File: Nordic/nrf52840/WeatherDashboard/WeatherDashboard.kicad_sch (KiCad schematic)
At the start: 0 parts

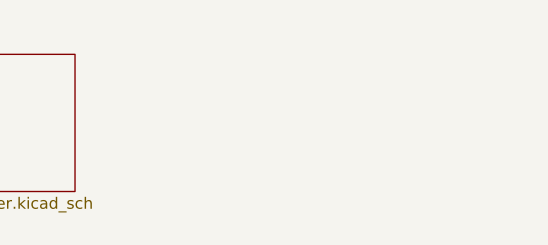
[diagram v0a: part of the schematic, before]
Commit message: power and display
Added power regulator and start populating display components
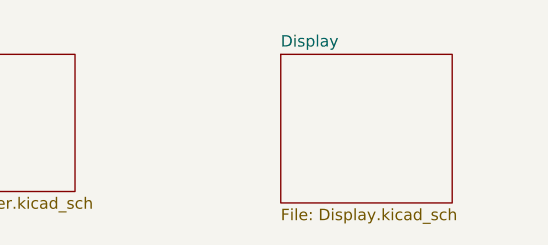
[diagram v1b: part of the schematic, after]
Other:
- added sheet Display (Display.kicad_sch)
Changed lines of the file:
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@@
+	)
+	(sheet
+		(at 181.61 77.47)
+		(size 19.05 16.51)
+		(exclude_from_sim no)
+		(in_bom yes)
+		(on_board yes)
+		(dnp no)
+		(fields_autoplaced yes)
+		(stroke
+			(width 0.1524)
+			(type solid)
+		)
+		(fill
+			(color 0 0 0 0.0000)
+		)
+		(property "Sheetname" "Display"
+			(at 181.61 76.7584 0)
+			(effects
+				(font
+					(size 1.27 1.27)
+				)
+				(justify left bottom)
+			)
+		)
+		(property "Sheetfile" "Display.kicad_sch"
+			(at 181.61 94.5646 0)
+			(effects
+				(font
+					(size 1.27 1.27)
+				)
+				(justify left top)
+			)
+		)
+		(instances
+			(project "WeatherDashboard"
+				(path "/189808bb-364f-4c11-a922-cc9d9f33a674"
+					(page "4")
+				)
+			)
+		)
 	)
 	(sheet

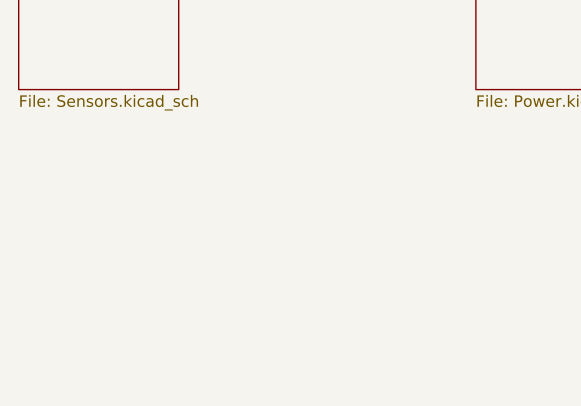
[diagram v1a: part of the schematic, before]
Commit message: pcie
added pcie connector
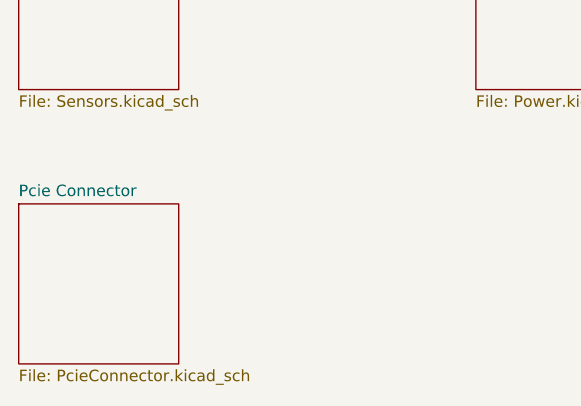
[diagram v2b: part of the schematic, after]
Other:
- added sheet Pcie Connector (PcieConnector.kicad_sch)
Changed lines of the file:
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@@
 	(paper "A4")
+	(sheet
+		(at 91.44 105.41)
+		(size 17.78 17.78)
+		(exclude_from_sim no)
+		(in_bom yes)
+		(on_board yes)
+		(dnp no)
+		(fields_autoplaced yes)
+		(stroke
+			(width 0.1524)
+			(type solid)
+		)
+		(fill
+			(color 0 0 0 0.0000)
+		)
+		(property "Sheetname" "Pcie Connector"
+			(at 91.44 104.6984 0)
+			(effects
+				(font
+					(size 1.27 1.27)
+				)
+				(justify left bottom)
+			)
+		)
+		(property "Sheetfile" "PcieConnector.kicad_sch"
+			(at 91.44 123.7746 0)
+			(effects
+				(font
+					(size 1.27 1.27)
+				)
+				(justify left top)
+			)
+		)
+		(instances
+			(project "WeatherDashboard"
+				(path "/189808bb-364f-4c11-a922-cc9d9f33a674"
+					(page "5")
+				)
+			)
+		)
+	)
 	(sheet
 		(at 142.24 77.47)

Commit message: pcie connector
Add connectins to the pcie connector
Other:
- sheet Display ports: added 3v3, 3v3_EN, BS, EPD_BUSY, EPD_DC, EPD_DIN, EPD_SCK, GND, TSCL, TSDA, ~{EPD_CS}, ~{EPD_RST}; removed none
- sheet Pcie Connector ports: added 3v3, EPD_BUSY, EPD_DC, EPD_DIN, EPD_SCK, GND, SCL, SDA, ~{EPD_CS}, ~{EPD_RST}; removed none
- sheet Power ports: added 3v3, GND; removed none
- sheet Sensors ports: added 3v3, GND, SCL, SDA; removed none

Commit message: Layout
layout update
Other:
- sheet Display ports: added none; removed BS
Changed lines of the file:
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@@
 	(paper "A4")
+	(junction
+		(at 152.4 73.66)
+		(diameter 0)
+		(color 0 0 0 0)
+	)
 	(junction
 		(at 138.43 100.33)
@@
 	(wire
 		(pts
+			(xy 152.4 76.2) (xy 152.4 73.66)
+		)
+		(stroke
+			(width 0)
+			(type default)
+		)
+	)
+	(wire
+		(pts
 			(xy 138.43 129.54) (xy 138.43 100.33)
 		)
@@
 	(wire
 		(pts
+			(xy 154.94 76.2) (xy 152.4 76.2)
+		)
+		(stroke
+			(width 0)
+			(type default)
+		)
+	)
+	(wire
+		(pts
 			(xy 135.89 102.87) (xy 154.94 102.87)
 		)
@@
 	(wire
 		(pts
-			(xy 130.81 73.66) (xy 154.94 73.66)
+			(xy 130.81 73.66) (xy 152.4 73.66)
 		)
 		(stroke
@@
 		(pts
 			(xy 124.46 102.87) (xy 135.89 102.87)
+		)
+		(stroke
+			(width 0)
+			(type default)
+		)
+	)
+	(wire
+		(pts
+			(xy 152.4 73.66) (xy 154.94 73.66)
 		)
 		(stroke
@@
 			(effects
 				(font
-					(size 1.27 1.27)
-				)
-				(justify left)
-			)
-		)
-		(pin "BS" input
-			(at 154.94 95.25 180)
-			(effects
-				(font

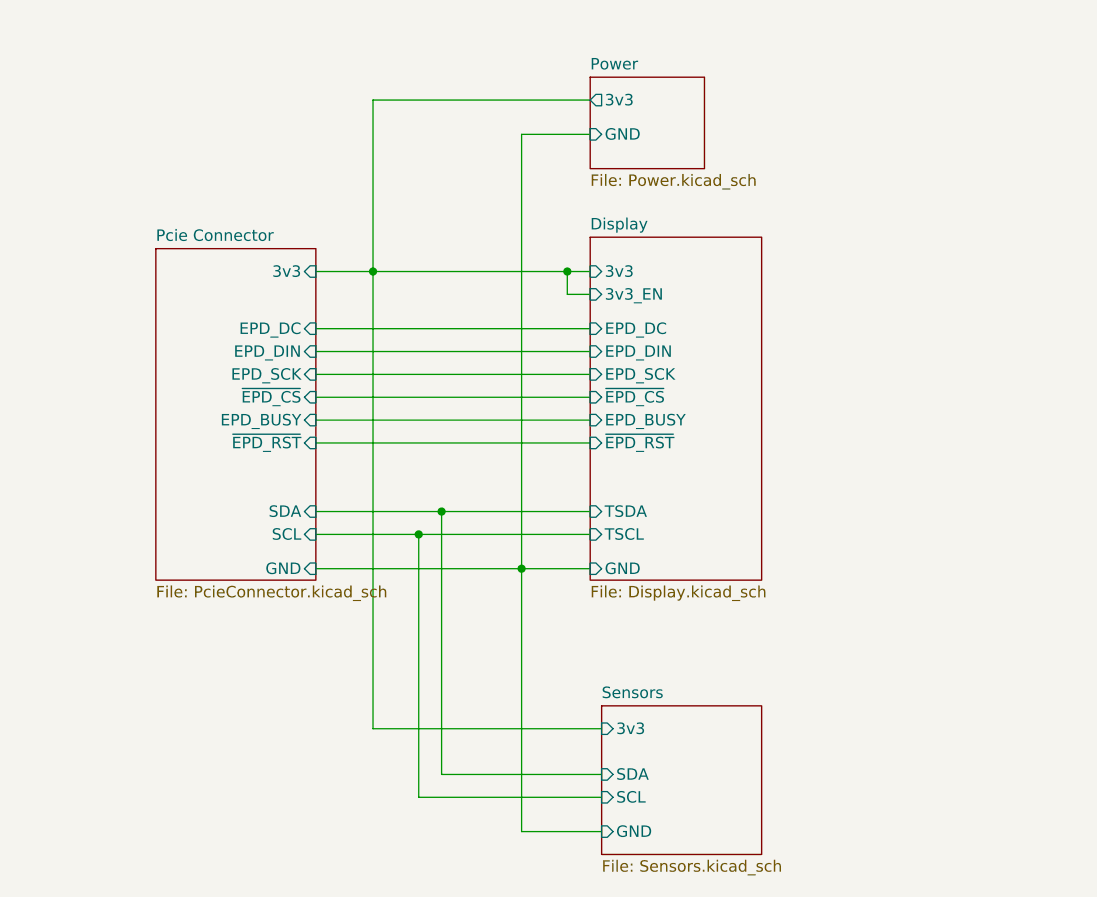
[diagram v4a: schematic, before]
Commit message: layout
Start weather station layout
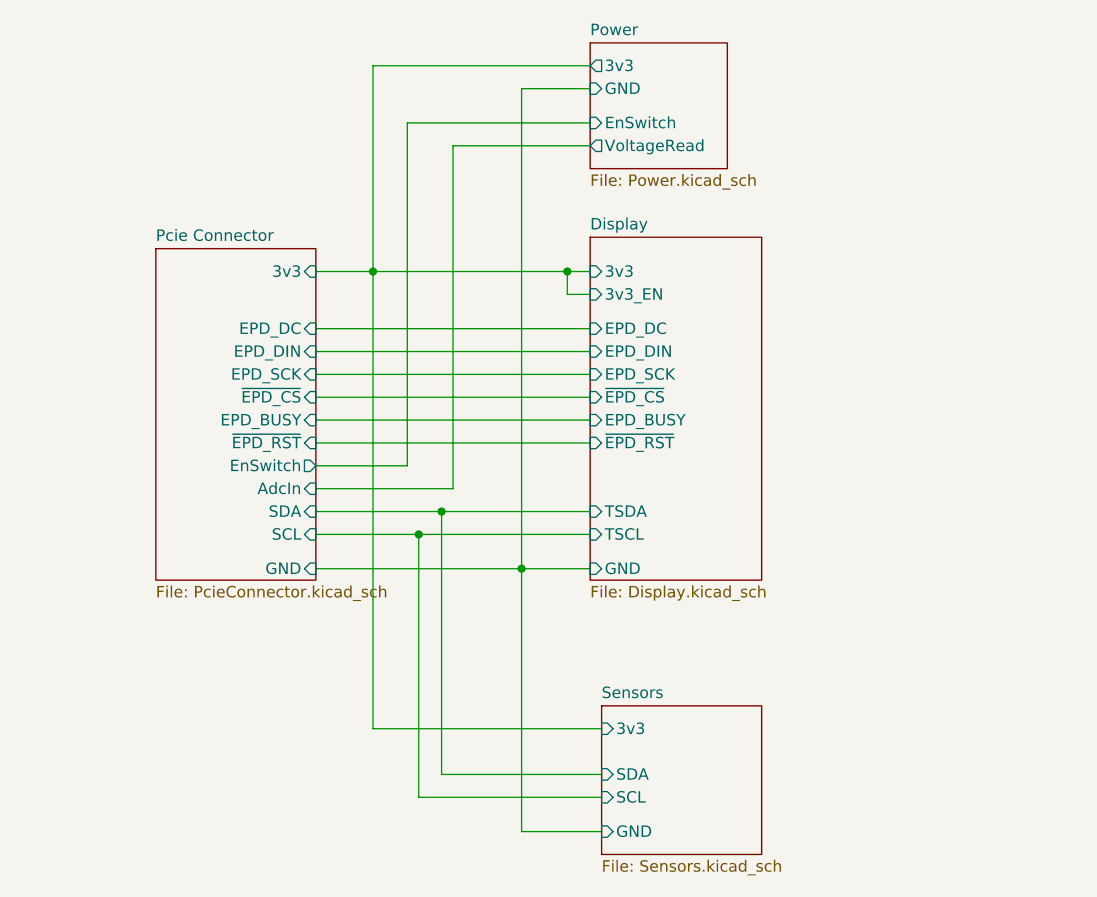
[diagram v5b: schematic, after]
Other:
- sheet Pcie Connector ports: added AdcIn, EnSwitch; removed none
- sheet Power ports: added EnSwitch, VoltageRead; removed none
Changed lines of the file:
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@@
 	(wire
 		(pts
-			(xy 154.94 58.42) (xy 147.32 58.42)
+			(xy 154.94 53.34) (xy 147.32 53.34)
+		)
+		(stroke
+			(width 0)
+			(type default)
+		)
+	)
+	(wire
+		(pts
+			(xy 139.7 59.69) (xy 154.94 59.69)
+		)
+		(stroke
+			(width 0)
+			(type default)
+		)
+	)
+	(wire
+		(pts
+			(xy 134.62 57.15) (xy 134.62 95.25)
 		)
 		(stroke
@@
 	(wire
 		(pts
-			(xy 154.94 54.61) (xy 130.81 54.61)
+			(xy 154.94 50.8) (xy 130.81 50.8)
 		)
 		(stroke
@@
 	(wire
 		(pts
-			(xy 147.32 58.42) (xy 147.32 106.68)
+			(xy 147.32 53.34) (xy 147.32 106.68)
 		)
 		(stroke
@@
 	(wire
 		(pts
+			(xy 124.46 97.79) (xy 139.7 97.79)
+		)
+		(stroke
+			(width 0)
+			(type default)
+		)
+	)
+	(wire
+		(pts
 			(xy 135.89 102.87) (xy 154.94 102.87)
 		)
@@
 	(wire
 		(pts
+			(xy 139.7 97.79) (xy 139.7 59.69)
+		)
+		(stroke
+			(width 0)
+			(type default)
+		)
+	)
+	(wire
+		(pts
 			(xy 124.46 92.71) (xy 154.94 92.71)
 		)
@@
 	(wire
 		(pts
-			(xy 130.81 54.61) (xy 130.81 73.66)
+			(xy 130.81 50.8) (xy 130.81 73.66)
 		)
 		(stroke
@@
 	(wire
 		(pts
+			(xy 154.94 57.15) (xy 134.62 57.15)
+		)
+		(stroke
+			(width 0)
+			(type default)
+		)
+	)
+	(wire
+		(pts
 			(xy 147.32 106.68) (xy 154.94 106.68)
+		)
+		(stroke
+			(width 0)
+			(type default)
+		)
+	)
+	(wire
+		(pts
+			(xy 134.62 95.25) (xy 124.46 95.25)
 		)
 		(stroke
@@
 			)
 		)
+		(pin "EnSwitch" output
+			(at 124.46 95.25 0)
+			(effects
+				(font
+					(size 1.27 1.27)
+				)
+				(justify right)
+			)
+		)
+		(pin "AdcIn" input
+			(at 124.46 97.79 0)
+			(effects
+				(font
+					(size 1.27 1.27)
+				)
+				(justify right)
+			)
+		)
 		(instances
 			(project "WeatherDashboard"
@@
 	)
 	(sheet
-		(at 154.94 52.07)
-		(size 12.7 10.16)
+		(at 154.94 48.26)
+		(size 15.24 13.97)
 		(exclude_from_sim no)
 		(in_bom yes)
@@
 		)
 		(property "Sheetname" "Power"
-			(at 154.94 51.3584 0)
+			(at 154.94 47.5484 0)
 			(effects
 				(font
@@
 		)
 		(pin "3v3" output
-			(at 154.94 54.61 180)
+			(at 154.94 50.8 180)
 			(effects
 				(font
@@
 		)
 		(pin "GND" input
-			(at 154.94 58.42 180)
-			(effects
-				(font
+			(at 154.94 53.34 180)
+			(effects
+				(font
+					(size 1.27 1.27)
+				)
+				(justify left)
+			)
+		)
+		(pin "EnSwitch" input
+			(at 154.94 57.15 180)
+			(effects
+				(font
+					(size 1.27 1.27)
+				)
+				(justify left)
+			)
+		)
+		(pin "VoltageRead" output
+			(at 154.94 59.69 180)
+			(effects
+				(font
